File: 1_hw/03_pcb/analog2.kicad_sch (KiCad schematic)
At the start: 0 parts

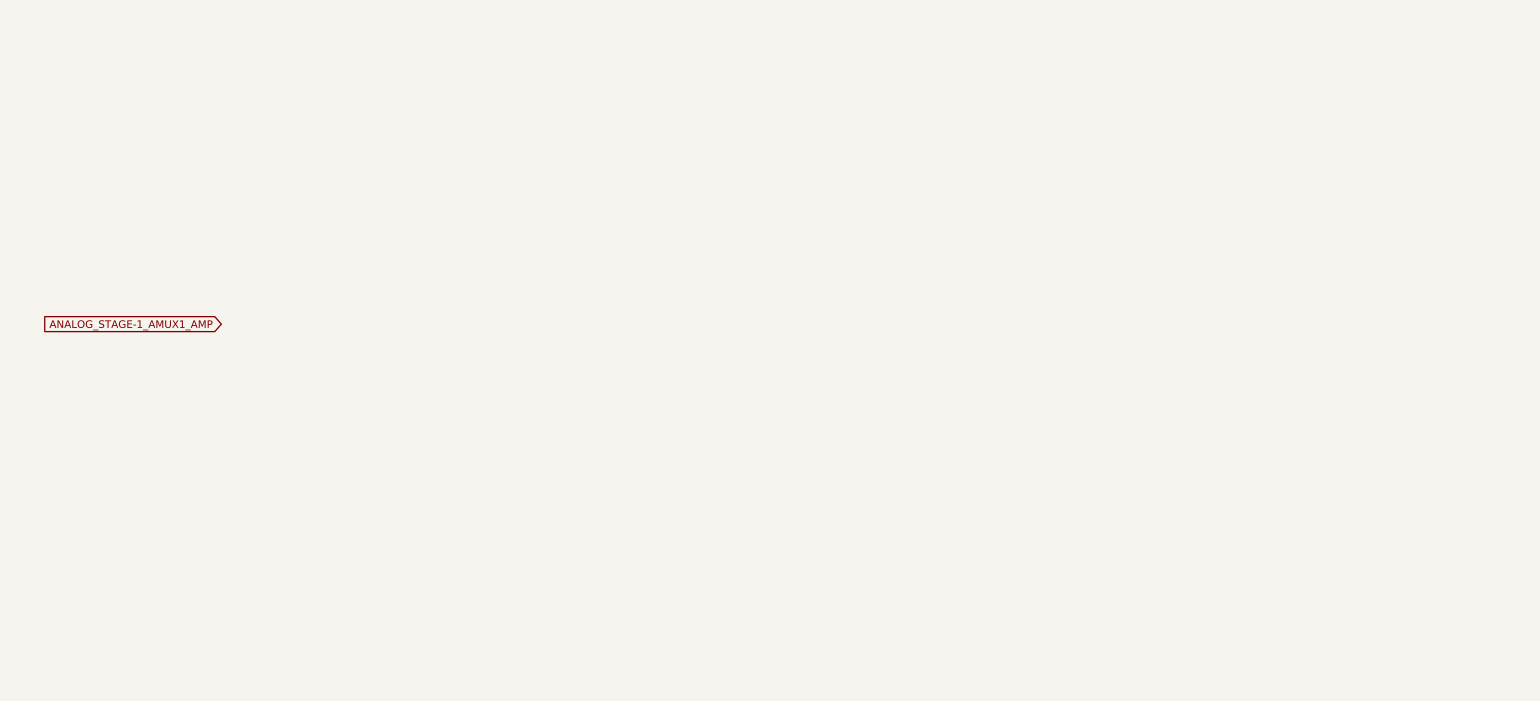
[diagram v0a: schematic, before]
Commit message: FEAT: Added Analog Stage 2 to Schematic. Some additional symbols (Pot, SPDT Analog MUX, etc.) added to Project.
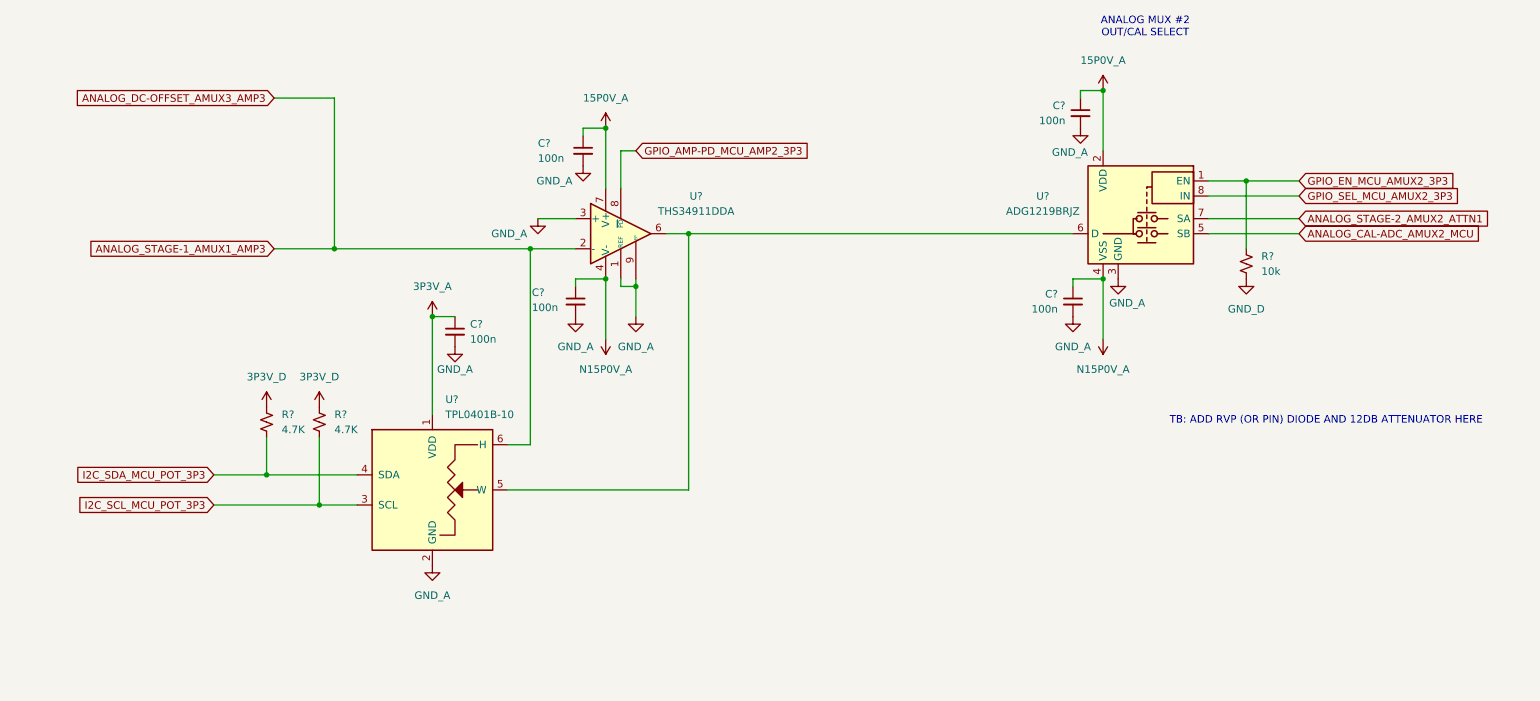
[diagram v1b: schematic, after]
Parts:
- added C? (x5): 100n, Capacitor_SMD:C_0603_1608Metric, symbol Device:C_Small
- added R?: 10k, Resistor_SMD:R_0603_1608Metric, symbol Device:R_Small_US
- added R? (x2): 4.7K, symbol Device:R_Small_US
- added U?: TPL0401B-10, Package_TO_SOT_SMD:Texas_R-PDSO-G6, symbol BRZK_POT:TPL0401B-10
- added U?: THS34911DDA, Package_SO:Texas_R-PDSO-G8_EP2.95x4.9mm_Mask2.4x3.1mm, symbol BRZK_OPAMP:THS34911DDA
- added U?: ADG1219BRJZ, TBD, symbol BRZK_MUX:ADG1219BRJZ
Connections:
- new net: U?.5 (W), U?.6, U?.6 (D)
- new net 15P0V_A: C?.1, C?.1, U?.2 (VDD), U?.7 (V+)
- new net 3P3V_A: C?.1, U?.1 (VDD)
- new net 3P3V_D: R?.2, R?.2
- new net ANALOG_CAL-ADC_AMUX2_MCU: U?.5 (SB)
- new net ANALOG_DC-OFFSET_AMUX3_AMP3: U?.2 (-), U?.6 (H)
- new net ANALOG_STAGE-2_AMUX2_ATTN1: U?.7 (SA)
- new net GND_A: C?.2, C?.2, C?.2, C?.2, C?.2, U?.1 (REF), U?.2 (GND), U?.3 (+), U?.3 (GND), U?.9 (EP)
- new net GND_D: R?.1
- new net GPIO_AMP-PD_MCU_AMP2_3P3: U?.8 (~{PD})
- new net GPIO_EN_MCU_AMUX2_3P3: R?.2, U?.1 (EN)
- new net GPIO_SEL_MCU_AMUX2_3P3: U?.8 (IN)
- new net I2C_SCL_MCU_POT_3P3: R?.1, U?.3 (SCL)
- new net I2C_SDA_MCU_POT_3P3: R?.1, U?.4 (SDA)
- new net N15P0V_A: C?.1, C?.1, U?.4 (V-), U?.4 (VSS)
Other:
- note added: "ANALOG MUX #2 OUT/CAL SELECT"
- note added: "TB: ADD RVP (OR PIN) DIODE AND 12DB ATTENUATOR HERE"

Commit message: FEAT: Added RVP Diode + Attenuation on the Cal Path.
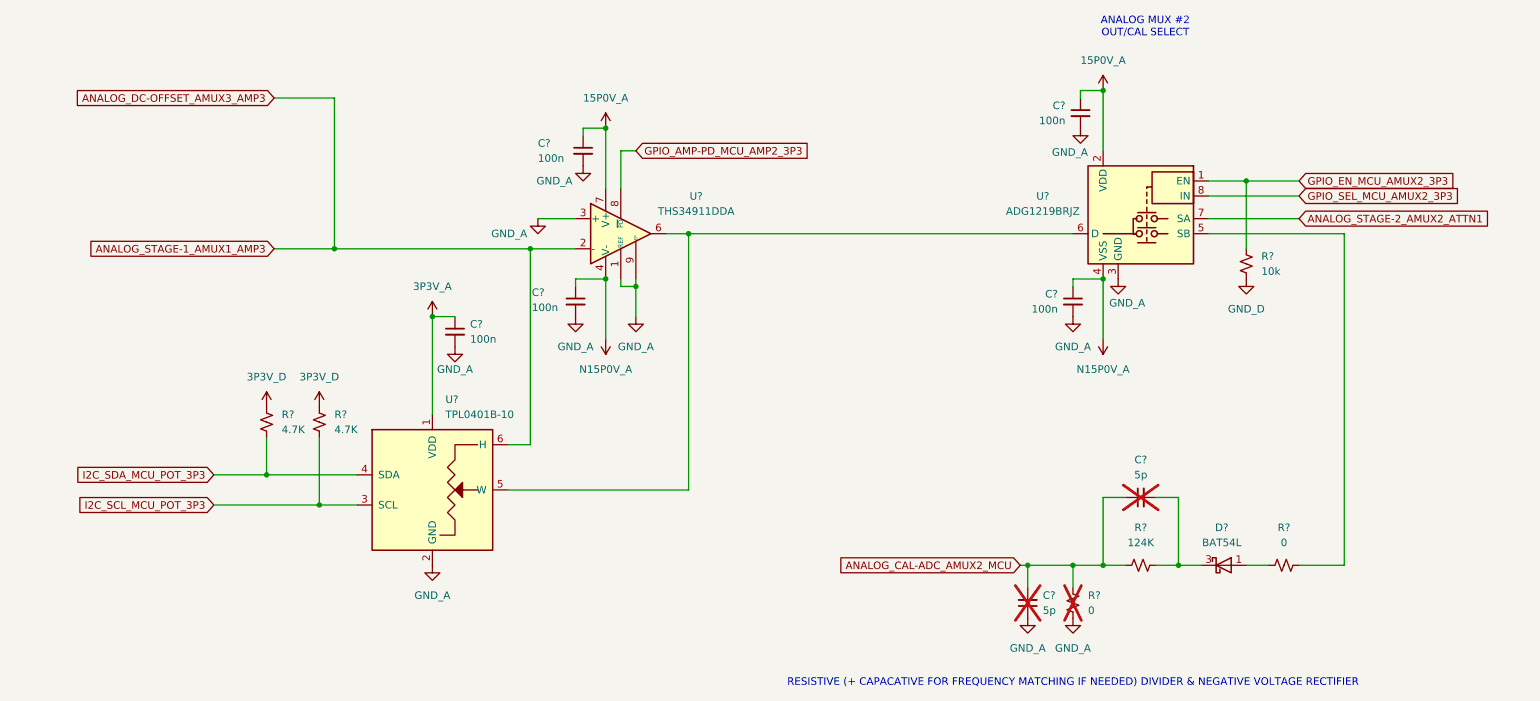
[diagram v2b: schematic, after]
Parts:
- added C? (x2): 5p, symbol Device:C_Small
- added D?: BAT54L, Package_TO_SOT_SMD:SOT-23, symbol BRZK_DIODE:BAT54L
- added R? (x2): 0, symbol Device:R_Small_US
- added R?: 124K, symbol Device:R_Small_US
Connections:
- net ANALOG_CAL-ADC_AMUX2_MCU: now also C?.1, C?.2, R?.1, R?.2; no longer U?.5 (SB)
- net GND_A: now also C?.1, R?.2
- new net: C?.2, D?.3 (K), R?.1
- new net: R?.1, U?.5 (SB)
- new net: D?.1 (A), R?.2
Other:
- note added: "RESISTIVE (+ CAPACATIVE FOR FREQUENCY MATCHING IF NEEDED) DIVIDER & NEGATIVE VOLTAGE RECTIFIER"
- note removed: "TB: ADD RVP (OR PIN) DIODE AND 12DB ATTENUATOR HERE"

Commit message: FEAT: Changed from two grounds (Digital + Analog) to Singular Ground IAW recommended Grounding Scheme.
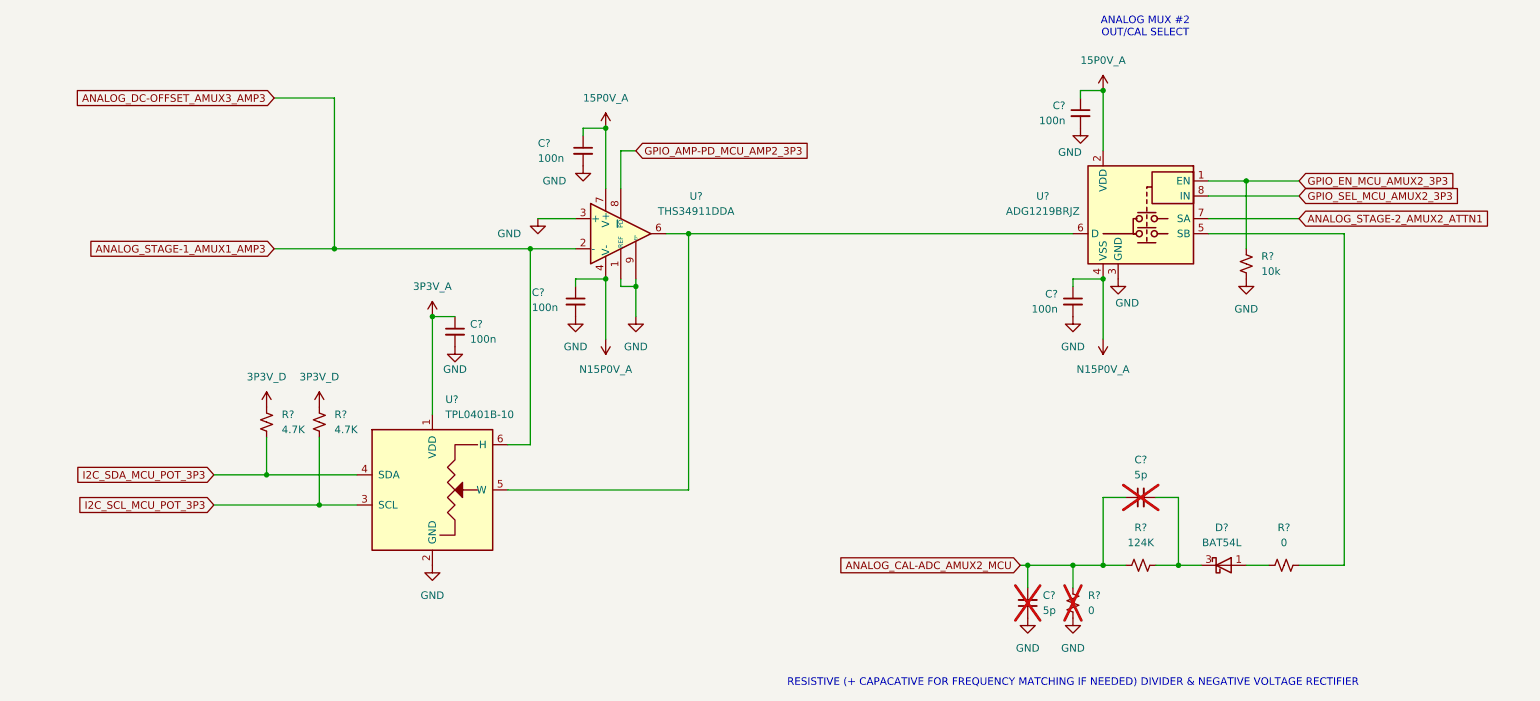
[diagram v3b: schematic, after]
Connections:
- net GND_D is gone; now on net GND: R?.1
- net GND_A renamed GND
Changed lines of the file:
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@@
 			)
 		)
-		(property "Value" "GND_A"
+		(property "Value" "GND"
 			(at 189.23 102.87 0)
 			(effects
@@
 			)
 		)
-		(property "Value" "GND_A"
+		(property "Value" "GND"
 			(at 189.23 153.67 0)
 			(effects
@@
 			)
 		)
-		(property "Value" "GND_A"
+		(property "Value" "GND"
 			(at 181.61 153.67 0)
 			(effects
@@
 			)
 		)
-		(property "Value" "GND_A"
+		(property "Value" "GND"
 			(at 188.722 70.104 0)
 			(effects
@@
 			)
 		)
-		(property "Value" "GND_A"
+		(property "Value" "GND"
 			(at 115.57 102.87 0)
 			(effects
@@
 			)
 		)
-		(property "Value" "GND_A"
+		(property "Value" "GND"
 			(at 101.854 74.93 0)
 			(effects
@@
 			)
 		)
-		(property "Value" "GND_D"
+		(property "Value" "GND"
 			(at 218.44 96.52 0)
 			(effects
@@
 			)
 		)
-		(property "Value" "GND_A"
+		(property "Value" "GND"
 			(at 198.374 95.504 0)
 			(effects
@@
 			)
 		)
-		(property "Value" "GND_A"
+		(property "Value" "GND"
 			(at 105.41 102.87 0)
 			(effects
@@
 			)
 		)
-		(property "Value" "GND_A"
+		(property "Value" "GND"
 			(at 81.28 144.78 0)
 			(effects
@@
 			)
 		)
-		(property "Value" "GND_A"
+		(property "Value" "GND"
 			(at 85.09 106.68 0)
 			(effects
@@
 			)
 		)
-		(property "Value" "GND_A"
+		(property "Value" "GND"
 			(at 94.234 83.82 0)
 			(effects

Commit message: FEAT: Added +15V and -15V Regulator. Replaced some Symbols to add additional Part Number Field.
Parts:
- removed D?: BAT54L, Package_TO_SOT_SMD:SOT-23, symbol BRZK_DIODE:BAT54L
- removed U?: THS34911DDA, Package_SO:Texas_R-PDSO-G8_EP2.95x4.9mm_Mask2.4x3.1mm, symbol BRZK_OPAMP:THS34911DDA
- added D?: BAT54L, Package_TO_SOT_SMD:SOT-23, symbol BRZK_DIODE:BAT54L
- added U?: THS3491, Package_SO:Texas_R-PDSO-G8_EP2.95x4.9mm_Mask2.4x3.1mm, symbol BRZK_OPAMP:THS349
- U?: Part Number (none) -> TPL0401B-10DCKR
- U?: footprint TBD -> BRZK_TBD; Part Number (none) -> ADG1219BRJZ
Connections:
- net 15P0V_A: now also U?.7 (V+)
- net ANALOG_DC-OFFSET_AMUX3_AMP3: now also U?.2 (-)
- net GND: now also U?.4 (VSS), U?.1 (REF), U?.3 (+), U?.9 (EP); no longer U?.3 (GND)
- net GPIO_AMP-PD_MCU_AMP2_3P3: now also U?.8 (~{PD})
- net N15P0V_A: now also U?.3 (GND), U?.4 (V-); no longer U?.4 (VSS)
- net at U?.5 (W), U?.6 (D): now also U?.6
- net at C?.2, R?.1: now also D?.3 (K)
- net at R?.2: now also D?.1 (A)
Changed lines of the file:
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@@
 	)
 	(junction
+		(at 110.49 91.44)
+		(diameter 0)
+		(color 0 0 0 0)
+	)
+	(junction
 		(at 181.61 139.7)
 		(diameter 0)
@@
 		(color 0 0 0 0)
 	)
-	(junction
-		(at 110.49 91.44)
-		(diameter 0)
-		(color 0 0 0 0)
-	)
 	(wire
 		(pts
@@
 			)
 		)
+		(property "Part Number" "TPL0401B-10DCKR "
+			(at 81.28 127 0)
+			(effects
+				(font
+					(size 1.27 1.27)
+				)
+				(hide yes)
+			)
+		)
 		(pin "6"
 		)
@@
 	)
 	(symbol
-		(lib_id "Device:C_Small")
-		(at 106.68 69.85 0)
+		(lib_id "BRZK_OPAMP:THS349")
+		(at 113.03 83.82 0)
 		(unit 1)
 		(exclude_from_sim no)
@@
 		(on_board yes)
 		(dnp no)
-		(property "Reference" "C?"
-			(at 99.06 68.58 0)
+		(property "Reference" "U?"
+			(at 119.38 76.962 0)
 			(effects
 				(font
 					(size 1.27 1.27)
 				)
-				(justify left)
 			)
 		)
-		(property "Value" "100n"
-			(at 99.06 71.12 0)
+		(property "Value" "THS3491"
+			(at 119.38 79.502 0)
 			(effects
 				(font
 					(size 1.27 1.27)
 				)
-				(justify left)
 			)
 		)
-		(property "Footprint" "Capacitor_SMD:C_0603_1608Metric"
-			(at 106.68 69.85 0)
+		(property "Footprint" "Package_SO:Texas_R-PDSO-G8_EP2.95x4.9mm_Mask2.4x3.1mm"
+			(at 113.03 99.06 0)
 			(effects
 				(font
@@
 			)
 		)
-		(property "Datasheet" "~"
-			(at 106.68 69.85 0)
+		(property "Datasheet" "http://www.ti.com/lit/ds/symlink/ths3491.pdf"
+			(at 116.84 80.01 0)
 			(effects
 				(font
@@
 			)
 		)
-		(property "Description" "Unpolarized capacitor, small symbol"
-			(at 106.68 69.85 0)
+		(property "Description" "900-MHz, 500-mA High-Power Output Current Feedback Operational Amplifier, SOIC-8"
+			(at 113.03 83.82 0)
 			(effects
 				(font
@@
 			)
 		)
-		(property "PN" "CL10B104JB8NNNC"
-			(at 106.68 69.85 0)
+		(property "Part Number" "THS3491IDDAR"
+			(at 127 80.0414 0)
 			(effects
 				(font
@@
 			)
 		)
-		(pin "2"
+		(pin "8"
 		)
 		(pin "1"
 		)
+		(pin "3"
+		)
+		(pin "4"
+		)
+		(pin "9"
+		)
+		(pin "6"
+		)
+		(pin "7"
+		)
+		(pin "2"
+		)
+		(pin "5"
+		)
 		(instances
-			(project "arb"
+			(project ""
 				(path "/866ef9be-3b01-4288-a6e0-a2357aa17e50/e46c6640-71a3-4b78-b602-0f6be9676e36"
-					(reference "C?")
+					(reference "U?")
 					(unit 1)
 				)
@@
 	)
 	(symbol
-		(lib_id "BRZK_OPAMP:THS34911DDA")
-		(at 113.03 83.82 0)
+		(lib_id "Device:C_Small")
+		(at 106.68 69.85 0)
 		(unit 1)
 		(exclude_from_sim no)
@@
 		(on_board yes)
 		(dnp no)
-		(fields_autoplaced yes)
-		(property "Reference" "U?"
-			(at 125.73 77.5014 0)
+		(property "Reference" "C?"
+			(at 99.06 68.58 0)
 			(effects
 				(font
 					(size 1.27 1.27)
 				)
+				(justify left)
 			)
 		)
-		(property "Value" "THS34911DDA"
-			(at 125.73 80.0414 0)
+		(property "Value" "100n"
+			(at 99.06 71.12 0)
 			(effects
 				(font
 					(size 1.27 1.27)
 				)
+				(justify left)
 			)
 		)
-		(property "Footprint" "Package_SO:Texas_R-PDSO-G8_EP2.95x4.9mm_Mask2.4x3.1mm"
-			(at 113.03 99.06 0)
+		(property "Footprint" "Capacitor_SMD:C_0603_1608Metric"
+			(at 106.68 69.85 0)
 			(effects
 				(font
@@
 			)
 		)
-		(property "Datasheet" "http://www.ti.com/lit/ds/symlink/ths3491.pdf"
-			(at 116.84 80.01 0)
+		(property "Datasheet" "~"
+			(at 106.68 69.85 0)
 			(effects
 				(font
@@
 			)
 		)
-		(property "Description" "900-MHz, 500-mA High-Power Output Current Feedback Operational Amplifier, SOIC-8"
-			(at 113.03 83.82 0)
+		(property "Description" "Unpolarized capacitor, small symbol"
+			(at 106.68 69.85 0)
 			(effects
 				(font
@@
 			)
 		)
-		(pin "8"
-		)
-		(pin "1"
-		)
-		(pin "9"
-		)
-		(pin "4"
+		(property "PN" "CL10B104JB8NNNC"
+			(at 106.68 69.85 0)
+			(effects
+				(font
+					(size 1.27 1.27)
+				)
+				(hide yes)
+			)
 		)
 		(pin "2"
 		)
-		(pin "6"
-		)
-		(pin "7"
-		)
-		(pin "3"
-		)
-		(pin "5"
+		(pin "1"
 		)
 		(instances
-			(project ""
+			(project "arb"
 				(path "/866ef9be-3b01-4288-a6e0-a2357aa17e50/e46c6640-71a3-4b78-b602-0f6be9676e36"
-					(reference "U?")
+					(reference "C?")
 					(unit 1)
 				)
@@
 	)
 	(symbol
+		(lib_id "BRZK_DIODE:BAT54L")
+		(at 214.63 139.7 0)
+		(unit 1)
+		(exclude_from_sim no)
+		(in_bom yes)
+		(on_board yes)
+		(dnp no)
+		(fields_autoplaced yes)
+		(property "Reference" "D?"
+			(at 214.3125 133.35 0)
+			(effects
+				(font
+					(size 1.27 1.27)
+				)
+			)
+		)
+		(property "Value" "BAT54L"
+			(at 214.3125 135.89 0)
+			(effects
+				(font
+					(size 1.27 1.27)
+				)
+			)
+		)
+		(property "Footprint" "Package_TO_SOT_SMD:SOT-23"
+			(at 214.63 144.145 0)
+			(effects
+				(font
+					(size 1.27 1.27)
+				)
+				(hide yes)
+			)
+		)
+		(property "Datasheet" "https://www.onsemi.com/download/data-sheet/pdf/bat54lt1-d.pdf"
+			(at 214.63 139.7 0)
+			(effects
+				(font
+					(size 1.27 1.27)
+				)
+				(hide yes)
+			)
+		)
+		(property "Description" "Schottky barrier diode, SOT-32"
+			(at 214.63 139.7 0)
+			(effects
+				(font
+					(size 1.27 1.27)
+				)
+				(hide yes)
+			)
+		)
+		(property "Part Number" "BAT54LT1G"
+			(at 214.63 139.7 0)
+			(effects
+				(font
+					(size 1.27 1.27)
+				)
+				(hide yes)
+			)
+		)
+		(pin "1"
+		)
+		(pin "3"
+		)
+		(pin "2"
+		)
+		(instances
+			(project "arb"
+				(path "/866ef9be-3b01-4288-a6e0-a2357aa17e50/e46c6640-71a3-4b78-b602-0f6be9676e36"
+					(reference "D?")
+					(unit 1)
+				)
+			)
+		)
+	)
+	(symbol
 		(lib_id "power:GND")
 		(at 105.41 97.79 0)
@@
 			)
 		)
-		(property "Footprint" "TBD"
+		(property "Footprint" "BRZK_TBD"
 			(at 201.93 86.36 0)
 			(effects
@@
 			)
 		)
+		(property "Part Number" "ADG1219BRJZ"
+			(at 201.93 83.82 0)
+			(effects
+				(font
+					(size 1.27 1.27)
+				)
+				(hide yes)
+			)
+		)
 		(pin "6"
 		)
@@
 					(unit 1)
 				)
-			)
-		)
-	)
-	(symbol
-		(lib_id "BRZK_DIODE:BAT54L")
-		(at 214.63 139.7 0)
-		(unit 1)
-		(exclude_from_sim no)
-		(in_bom yes)
-		(on_board yes)
-		(dnp no)
-		(fields_autoplaced yes)
-		(property "Reference" "D?"
-			(at 214.3125 133.35 0)
-			(effects
-				(font
-					(size 1.27 1.27)
-				)
-			)
-		)
-		(property "Value" "BAT54L"
-			(at 214.3125 135.89 0)
-			(effects
-				(font
-					(size 1.27 1.27)
-				)
-			)
-		)
-		(property "Footprint" "Package_TO_SOT_SMD:SOT-23"
-			(at 214.63 144.145 0)
-			(effects
-				(font
-					(size 1.27 1.27)
-				)
-				(hide yes)
-			)
-		)
-		(property "Datasheet" "https://www.onsemi.com/download/data-sheet/pdf/bat54lt1-d.pdf"
-			(at 214.63 139.7 0)
-			(effects
-				(font
-					(size 1.27 1.27)
-				)
-				(hide yes)
-			)
-		)
-		(property "Description" "Schottky barrier diode, SOT-32"
-			(at 214.63 139.7 0)
-			(effects
-				(font
-					(size 1.27 1.27)
-				)
-				(hide yes)
-			)
-		)
-		(pin "1"
-		)
-		(pin "3"
-		)
-		(pin "2"
-		)
-		(instances
-			(project ""
-				(path "/866ef9be-3b01-4288-a6e0-a2357aa17e50/e46c6640-71a3-4b78-b602-0f6be9676e36"
-					(reference "D?")
-					(unit 1)
-				)
